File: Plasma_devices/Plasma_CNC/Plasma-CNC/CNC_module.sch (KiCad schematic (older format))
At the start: 0 parts

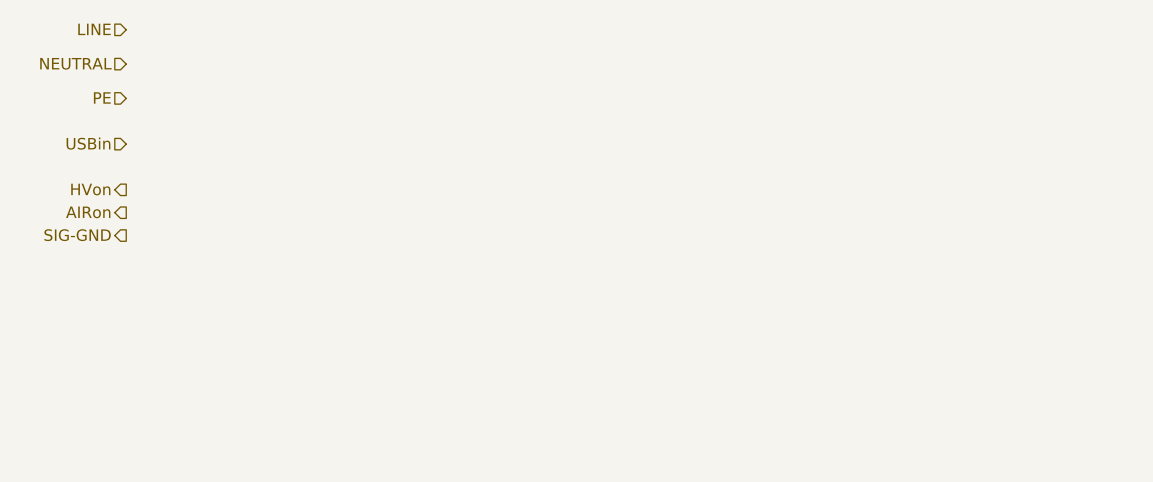
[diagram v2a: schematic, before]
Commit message: CNC module included
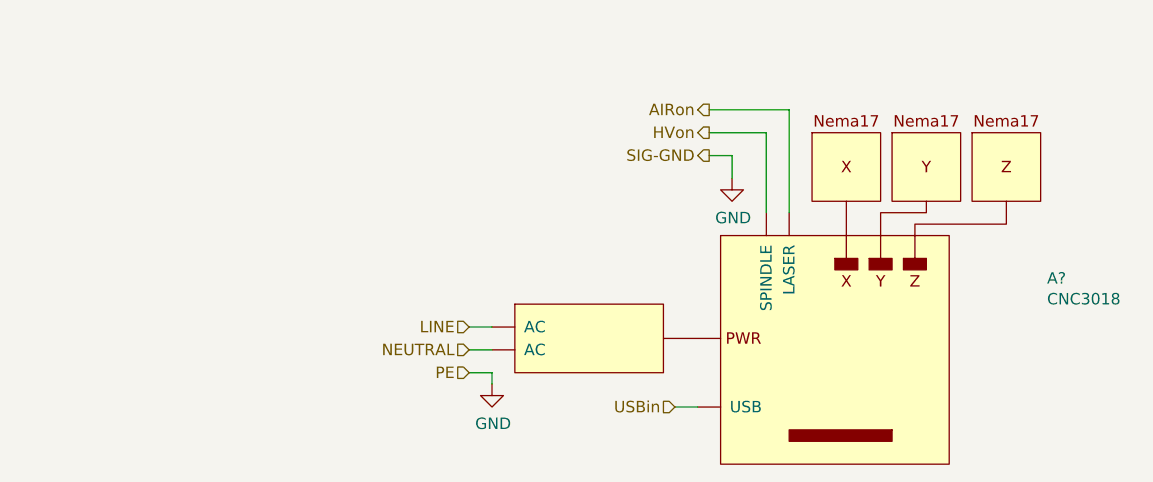
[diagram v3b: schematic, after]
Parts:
- added A?: CNC3018, symbol Plasma-CNC:CNC3018
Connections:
- net AIRon: now also A?.~ (USB)
- net HVon: now also A?.~ (USB)
- net LINE: now also A?.~ (USB)
- net NEUTRAL: now also A?.~ (USB)
- net USBin: now also A?.~ (USB)
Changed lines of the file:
@@
 Comment2 "Plasma Center"
 Comment3 ""
-Comment4 ""
+Comment4 "Sebastian Dahle, Bojan Gospodarić"
 $EndDescr
-Text HLabel 1450 1100 0    50   Input ~ 0
+Text HLabel 2950 2400 0    50   Input ~ 0
 LINE
-Text HLabel 1450 1250 0    50   Input ~ 0
+Text HLabel 2950 2500 0    50   Input ~ 0
 NEUTRAL
-Text HLabel 1450 1400 0    50   Input ~ 0
+Text HLabel 2950 2600 0    50   Input ~ 0
 PE
-Text HLabel 1450 1800 0    50   Output ~ 0
+Text HLabel 4000 1550 0    50   Output ~ 0
 HVon
-Text HLabel 1450 1900 0    50   Output ~ 0
+Text HLabel 4000 1450 0    50   Output ~ 0
 AIRon
-Text HLabel 1450 2000 0    50   Output ~ 0
+Text HLabel 4000 1650 0    50   Output ~ 0
 SIG-GND
-Text HLabel 1450 1600 0    50   Input ~ 0
+Text HLabel 3850 2750 0    50   Input ~ 0
 USBin
+$Comp
+L Plasma-CNC:CNC3018 A?
+U 1 1 5F6F66CE
+P 4550 2500
+F 0 "A?" H 5478 2813 50  0000 L CNN
+F 1 "CNC3018" H 5478 2722 50  0000 L CNN
+F 2 "" H 3950 3200 50  0001 C CNN
+F 3 "" H 3950 3200 50  0001 C CNN
+	1    4550 2500
+	1    0    0    -1
+$EndComp
+$Comp
+L power:GND #PWR?
+U 1 1 5F6F7A1F
+P 4100 1750
+F 0 "#PWR?" H 4100 1500 50  0001 C CNN
+F 1 "GND" H 4105 1577 50  0000 C CNN
+F 2 "" H 4100 1750 50  0001 C CNN
+F 3 "" H 4100 1750 50  0001 C CNN
+	1    4100 1750
+	1    0    0    -1
+$EndComp
+$Comp
+L power:GND #PWR?
+U 1 1 5F6F7AA8
+P 3050 2650
+F 0 "#PWR?" H 3050 2400 50  0001 C CNN
+F 1 "GND" H 3055 2477 50  0000 C CNN
+F 2 "" H 3050 2650 50  0001 C CNN
+F 3 "" H 3050 2650 50  0001 C CNN
+	1    3050 2650
+	1    0    0    -1
+$EndComp
+Wire Wire Line
+	3850 2750 3950 2750
+Wire Wire Line
+	3050 2650 3050 2600
+Wire Wire Line
+	3050 2600 2950 2600
+Wire Wire Line
+	2950 2500 3050 2500
+Wire Wire Line
+	3050 2400 2950 2400
+Wire Wire Line
+	4000 1650 4100 1650
+Wire Wire Line
+	4100 1650 4100 1750
+Wire Wire Line
+	4000 1550 4250 1550
+Wire Wire Line
+	4250 1550 4250 1900
+Wire Wire Line
+	4000 1450 4350 1450
+Wire Wire Line
+	4350 1450 4350 1900
 $EndSCHEMATC
